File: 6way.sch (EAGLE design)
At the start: 15 parts

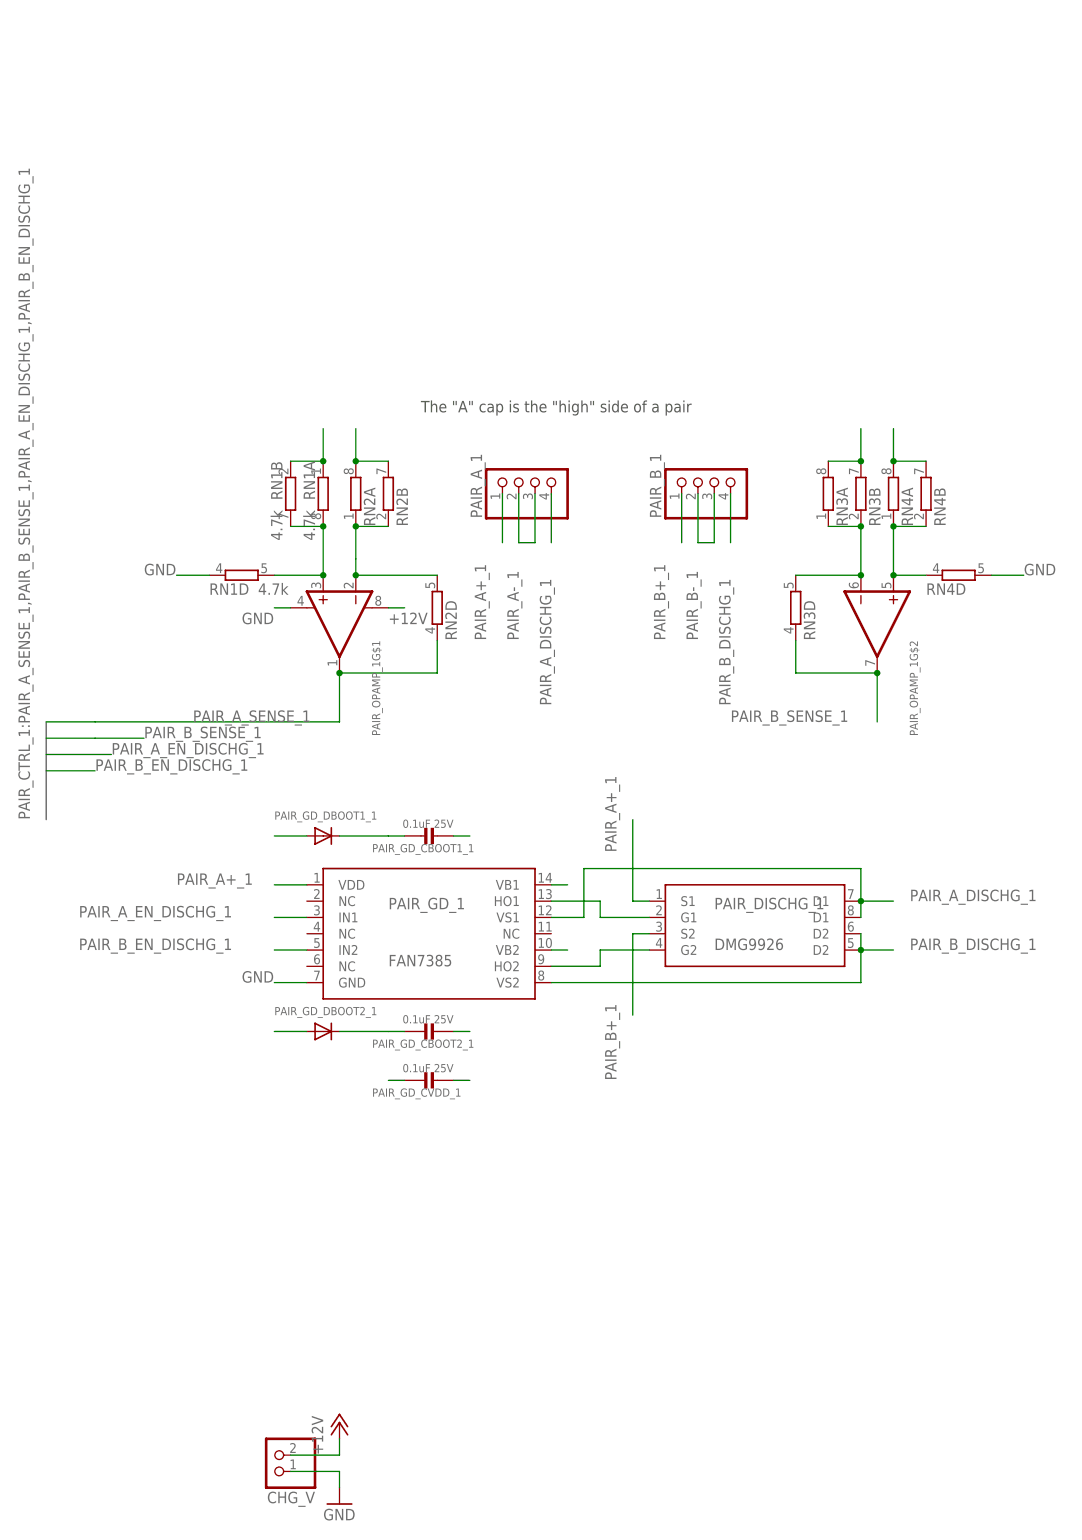
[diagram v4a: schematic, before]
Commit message: use solder jumper with trace to separate small-signal nets from the high-current ones
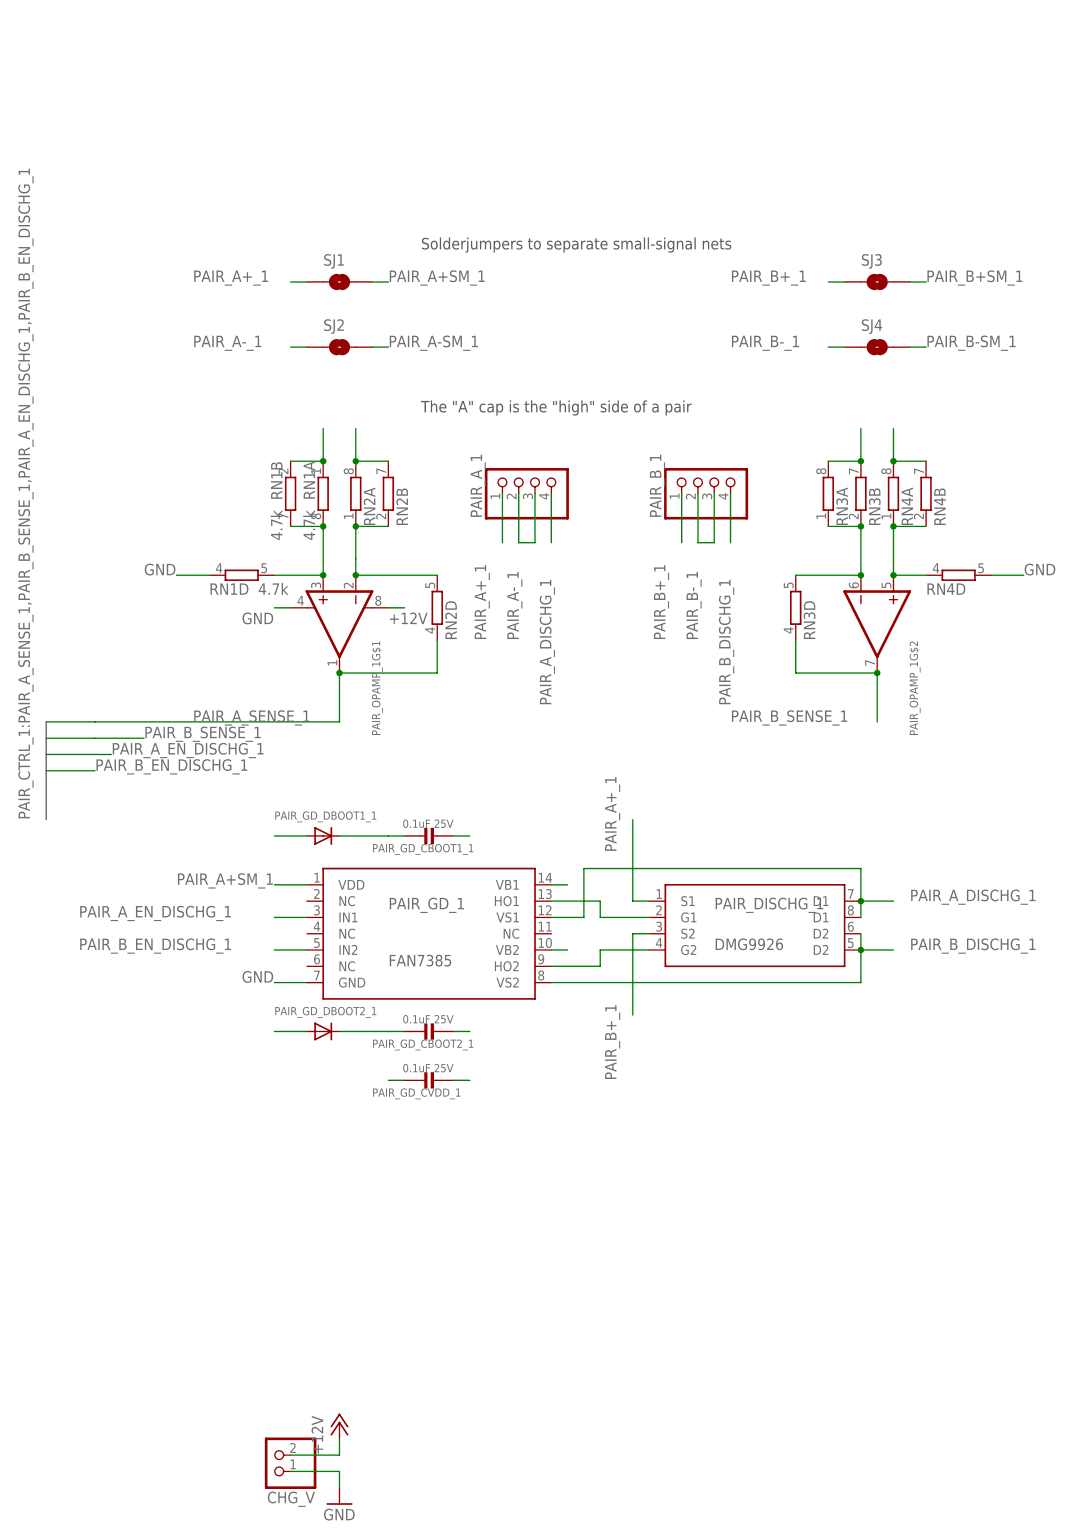
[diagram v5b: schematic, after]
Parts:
- added SJ1, SJ2, SJ3, SJ4: SOLDERJUMPERTRACE, SparkFun-Passives:SOLDERJUMPERTRACE
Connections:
- removed net PAIR_1_A_+: RN1A.1, RN1B.1
- new net PAIR_A+SM_1: PAIR_GD_1.VDD, PAIR_GD_DBOOT1_1.A, PAIR_GD_DBOOT2_1.A, RN1A.1, RN1B.1, SJ1.2
- new net PAIR_A-SM_1: RN2A.2, RN2B.2, SJ2.2
- new net PAIR_B+SM_1: RN4A.2, RN4B.2, SJ3.2
- new net PAIR_B-SM_1: RN3A.2, RN3B.2, SJ4.2
- net PAIR_A+_1: now also SJ1.1; no longer PAIR_GD_1.VDD, PAIR_GD_DBOOT1_1.A, PAIR_GD_DBOOT2_1.A
- net PAIR_A-_1: now also SJ2.1; no longer RN2A.2, RN2B.2
- net PAIR_B+_1: now also SJ3.1; no longer RN4A.2, RN4B.2
- net PAIR_B-_1: now also SJ4.1; no longer RN3A.2, RN3B.2
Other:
- note added: "Solderjumpers to separate small-signal nets"
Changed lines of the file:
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@@
 <layer number="111" name="MPL" color="7" fill="1" visible="yes" active="yes"/>
 <layer number="112" name="tSilk" color="7" fill="1" visible="yes" active="yes"/>
+<layer number="116" name="Patch_BOT" color="9" fill="4" visible="no" active="yes"/>
 <layer number="121" name="sName" color="7" fill="1" visible="yes" active="yes"/>
 <layer number="122" name="_bPlace" color="7" fill="1" visible="yes" active="yes"/>
@@
 <layer number="204" name="204bmp" color="7" fill="1" visible="yes" active="yes"/>
 <layer number="205" name="205bmp" color="7" fill="1" visible="yes" active="yes"/>
+<layer number="206" name="206bmp" color="7" fill="10" visible="no" active="yes"/>
+<layer number="207" name="207bmp" color="8" fill="10" visible="no" active="yes"/>
+<layer number="208" name="208bmp" color="9" fill="10" visible="no" active="yes"/>
+<layer number="209" name="209bmp" color="7" fill="1" visible="no" active="yes"/>
+<layer number="210" name="210bmp" color="7" fill="1" visible="no" active="yes"/>
+<layer number="211" name="211bmp" color="7" fill="1" visible="no" active="yes"/>
+<layer number="212" name="212bmp" color="7" fill="1" visible="no" active="yes"/>
+<layer number="213" name="213bmp" color="7" fill="1" visible="no" active="yes"/>
+<layer number="214" name="214bmp" color="7" fill="1" visible="no" active="yes"/>
+<layer number="215" name="215bmp" color="7" fill="1" visible="no" active="yes"/>
+<layer number="216" name="216bmp" color="7" fill="1" visible="no" active="yes"/>
+<layer number="217" name="217bmp" color="18" fill="1" visible="no" active="no"/>
+<layer number="218" name="218bmp" color="19" fill="1" visible="no" active="no"/>
+<layer number="219" name="219bmp" color="20" fill="1" visible="no" active="no"/>
+<layer number="220" name="220bmp" color="21" fill="1" visible="no" active="no"/>
+<layer number="221" name="221bmp" color="22" fill="1" visible="no" active="no"/>
+<layer number="222" name="222bmp" color="23" fill="1" visible="no" active="no"/>
+<layer number="223" name="223bmp" color="24" fill="1" visible="no" active="no"/>
+<layer number="224" name="224bmp" color="25" fill="1" visible="no" active="no"/>
 <layer number="248" name="Housing" color="7" fill="1" visible="yes" active="yes"/>
 <layer number="249" name="Edge" color="7" fill="1" visible="yes" active="yes"/>
@@
 <part name="PAIR_GD_DBOOT2_1" library="microbuilder" deviceset="DIODE" device="SOT23_WIDE"/>
 <part name="PAIR_GD_DBOOT1_1" library="microbuilder" deviceset="DIODE" device="SOT23_WIDE"/>
+<part name="SJ1" library="SparkFun-Passives" deviceset="SOLDERJUMPER" device="TRACE"/>
+<part name="SJ2" library="SparkFun-Passives" deviceset="SOLDERJUMPER" device="TRACE"/>
+<part name="SJ3" library="SparkFun-Passives" deviceset="SOLDERJUMPER" device="TRACE"/>
+<part name="SJ4" library="SparkFun-Passives" deviceset="SOLDERJUMPER" device="TRACE"/>
 </parts>
 <sheets>
@@
 <plain>
 <text x="2.54" y="127" size="1.778" layer="97">The "A" cap is the "high" side of a pair</text>
+<text x="2.54" y="152.4" size="1.778" layer="97">Solderjumpers to separate small-signal nets</text>
 </plain>
 <instances>
@@
 <attribute name="VALUE" x="-15.24" y="57.15" size="1.27" layer="96"/>
 </instance>
+<instance part="SJ1" gate="1" x="-10.16" y="147.32" smashed="yes">
+<attribute name="NAME" x="-12.7" y="149.86" size="1.778" layer="95"/>
+</instance>
+<instance part="SJ2" gate="1" x="-10.16" y="137.16" smashed="yes">
+<attribute name="NAME" x="-12.7" y="139.7" size="1.778" layer="95"/>
+</instance>
+<instance part="SJ3" gate="1" x="73.66" y="147.32" smashed="yes">
+<attribute name="NAME" x="71.12" y="149.86" size="1.778" layer="95"/>
+</instance>
+<instance part="SJ4" gate="1" x="73.66" y="137.16" smashed="yes">
+<attribute name="NAME" x="71.12" y="139.7" size="1.778" layer="95"/>
+</instance>
 </instances>
 <busses>
@@
 </segment>
 </net>
-<net name="PAIR_1_A_+" class="2">
+<net name="PAIR_A+SM_1" class="2">
 <segment>
 <pinref part="RN1" gate="B" pin="1"/>
@@
 <wire x1="-12.7" y1="119.38" x2="-12.7" y2="124.46" width="0.1524" layer="91"/>
 <junction x="-12.7" y="119.38"/>
+</segment>
+<segment>
+<pinref part="SJ1" gate="1" pin="2"/>
+<wire x1="-5.08" y1="147.32" x2="-2.54" y2="147.32" width="0.1524" layer="91"/>
+<label x="-2.54" y="147.32" size="1.778" layer="95"/>
+</segment>
+<segment>
+<pinref part="PAIR_GD_1" gate="G$1" pin="VDD"/>
+<wire x1="-15.24" y1="53.34" x2="-20.32" y2="53.34" width="0.1524" layer="91"/>
+<label x="-35.56" y="53.34" size="1.778" layer="95"/>
+</segment>
+<segment>
+<pinref part="PAIR_GD_DBOOT1_1" gate="G$1" pin="A"/>
+<wire x1="-15.24" y1="60.96" x2="-20.32" y2="60.96" width="0.1524" layer="91"/>
+</segment>
+<segment>
+<pinref part="PAIR_GD_DBOOT2_1" gate="G$1" pin="A"/>
+<wire x1="-15.24" y1="30.48" x2="-20.32" y2="30.48" width="0.1524" layer="91"/>
 </segment>
 </net>
@@
 </segment>
 <segment>
-<pinref part="RN2" gate="A" pin="2"/>
-<pinref part="RN2" gate="B" pin="2"/>
-<wire x1="-7.62" y1="119.38" x2="-2.54" y2="119.38" width="0.1524" layer="91"/>
-<wire x1="-7.62" y1="119.38" x2="-7.62" y2="124.46" width="0.1524" layer="91"/>
-<junction x="-7.62" y="119.38"/>
+<pinref part="SJ2" gate="1" pin="1"/>
+<wire x1="-15.24" y1="137.16" x2="-17.78" y2="137.16" width="0.1524" layer="91"/>
+<label x="-33.02" y="137.16" size="1.778" layer="95"/>
 </segment>
 </net>
@@
 </segment>
 <segment>
-<pinref part="PAIR_GD_1" gate="G$1" pin="VDD"/>
-<wire x1="-15.24" y1="53.34" x2="-20.32" y2="53.34" width="0.1524" layer="91"/>
-<label x="-35.56" y="53.34" size="1.778" layer="95"/>
-</segment>
-<segment>
 <pinref part="PAIR_GD_CVDD_1" gate="G$1" pin="P$2"/>
 <wire x1="0" y1="22.86" x2="-2.54" y2="22.86" width="0.1524" layer="91"/>
 </segment>
 <segment>
-<pinref part="PAIR_GD_DBOOT1_1" gate="G$1" pin="A"/>
-<wire x1="-15.24" y1="60.96" x2="-20.32" y2="60.96" width="0.1524" layer="91"/>
-</segment>
-<segment>
-<pinref part="PAIR_GD_DBOOT2_1" gate="G$1" pin="A"/>
-<wire x1="-15.24" y1="30.48" x2="-20.32" y2="30.48" width="0.1524" layer="91"/>
+<pinref part="SJ1" gate="1" pin="1"/>
+<wire x1="-15.24" y1="147.32" x2="-17.78" y2="147.32" width="0.1524" layer="91"/>
+<label x="-33.02" y="147.32" size="1.778" layer="95"/>
 </segment>
 </net>
@@
 </segment>
 <segment>
-<pinref part="RN3" gate="B" pin="2"/>
-<pinref part="RN3" gate="A" pin="2"/>
-<wire x1="71.12" y1="119.38" x2="66.04" y2="119.38" width="0.1524" layer="91"/>
-<wire x1="71.12" y1="119.38" x2="71.12" y2="124.46" width="0.1524" layer="91"/>
-<junction x="71.12" y="119.38"/>
+<pinref part="SJ4" gate="1" pin="1"/>
+<wire x1="68.58" y1="137.16" x2="66.04" y2="137.16" width="0.1524" layer="91"/>
+<label x="50.8" y="137.16" size="1.778" layer="95"/>
 </segment>
 </net>
@@
 </segment>
 <segment>
-<pinref part="RN4" gate="B" pin="2"/>
-<pinref part="RN4" gate="A" pin="2"/>
-<wire x1="81.28" y1="119.38" x2="76.2" y2="119.38" width="0.1524" layer="91"/>
-<wire x1="76.2" y1="119.38" x2="76.2" y2="124.46" width="0.1524" layer="91"/>
-<junction x="76.2" y="119.38"/>
-</segment>
-<segment>
 <pinref part="PAIR_DISCHG_1" gate="G$1" pin="S2"/>
 <wire x1="38.1" y1="45.72" x2="35.56" y2="45.72" width="0.1524" layer="91"/>
 <wire x1="35.56" y1="45.72" x2="35.56" y2="33.02" width="0.1524" layer="91"/>
 <label x="33.02" y="22.86" size="1.778" layer="95" rot="R90"/>
+</segment>
+<segment>
+<pinref part="SJ3" gate="1" pin="1"/>
+<wire x1="68.58" y1="147.32" x2="66.04" y2="147.32" width="0.1524" layer="91"/>
+<label x="50.8" y="147.32" size="1.778" layer="95"/>
 </segment>
 </net>
@@
 </segment>
 </net>
+<net name="PAIR_A-SM_1" class="2">
+<segment>
+<pinref part="RN2" gate="A" pin="2"/>
+<pinref part="RN2" gate="B" pin="2"/>
+<wire x1="-7.62" y1="119.38" x2="-2.54" y2="119.38" width="0.1524" layer="91"/>
+<wire x1="-7.62" y1="119.38" x2="-7.62" y2="124.46" width="0.1524" layer="91"/>
+<junction x="-7.62" y="119.38"/>
+</segment>
+<segment>
+<pinref part="SJ2" gate="1" pin="2"/>
+<wire x1="-5.08" y1="137.16" x2="-2.54" y2="137.16" width="0.1524" layer="91"/>
+<label x="-2.54" y="137.16" size="1.778" layer="95"/>
+</segment>
+</net>
+<net name="PAIR_B-SM_1" class="2">
+<segment>
+<pinref part="RN3" gate="B" pin="2"/>
+<pinref part="RN3" gate="A" pin="2"/>
+<wire x1="71.12" y1="119.38" x2="66.04" y2="119.38" width="0.1524" layer="91"/>
+<wire x1="71.12" y1="119.38" x2="71.12" y2="124.46" width="0.1524" layer="91"/>
+<junction x="71.12" y="119.38"/>
+</segment>
+<segment>
+<pinref part="SJ4" gate="1" pin="2"/>
+<wire x1="78.74" y1="137.16" x2="81.28" y2="137.16" width="0.1524" layer="91"/>
+<label x="81.28" y="137.16" size="1.778" layer="95"/>
+</segment>
+</net>
+<net name="PAIR_B+SM_1" class="2">
+<segment>
+<pinref part="RN4" gate="B" pin="2"/>
+<pinref part="RN4" gate="A" pin="2"/>
+<wire x1="81.28" y1="119.38" x2="76.2" y2="119.38" width="0.1524" layer="91"/>
+<wire x1="76.2" y1="119.38" x2="76.2" y2="124.46" width="0.1524" layer="91"/>
+<junction x="76.2" y="119.38"/>
+</segment>
+<segment>
+<pinref part="SJ3" gate="1" pin="2"/>
+<wire x1="78.74" y1="147.32" x2="81.28" y2="147.32" width="0.1524" layer="91"/>
+<label x="81.28" y="147.32" size="1.778" layer="95"/>
+</segment>
+</net>
